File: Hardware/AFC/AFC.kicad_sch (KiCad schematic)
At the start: 5 parts, among them J1 Barrel_Jack_Switch, J2 Conn_Coaxial, J3 Conn_Coaxial, J4 Conn_Coaxial, J5 Conn_Coaxial

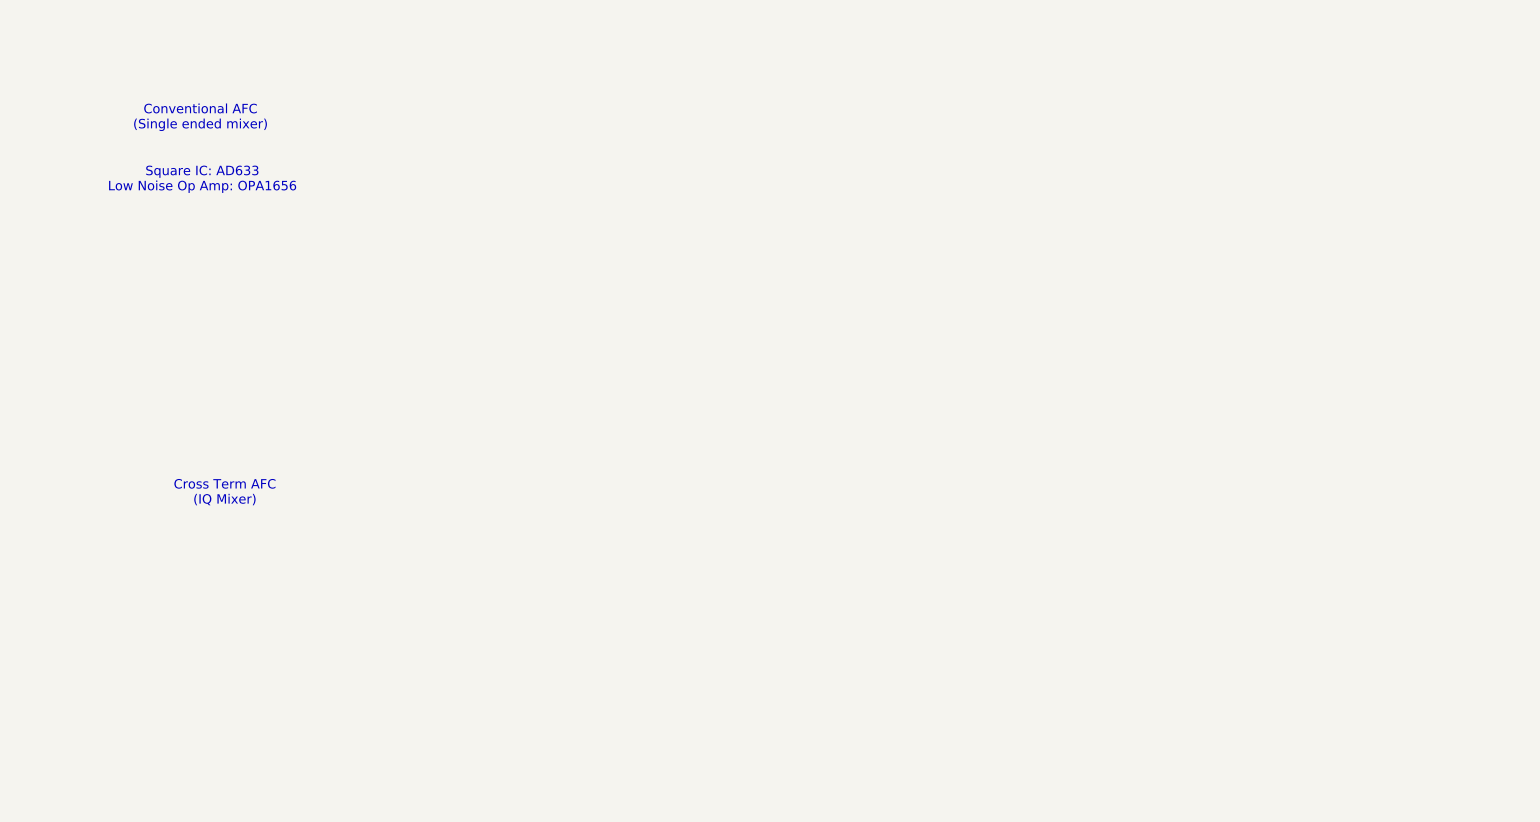
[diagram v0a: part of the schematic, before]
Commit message: Updating Schematic for AFC
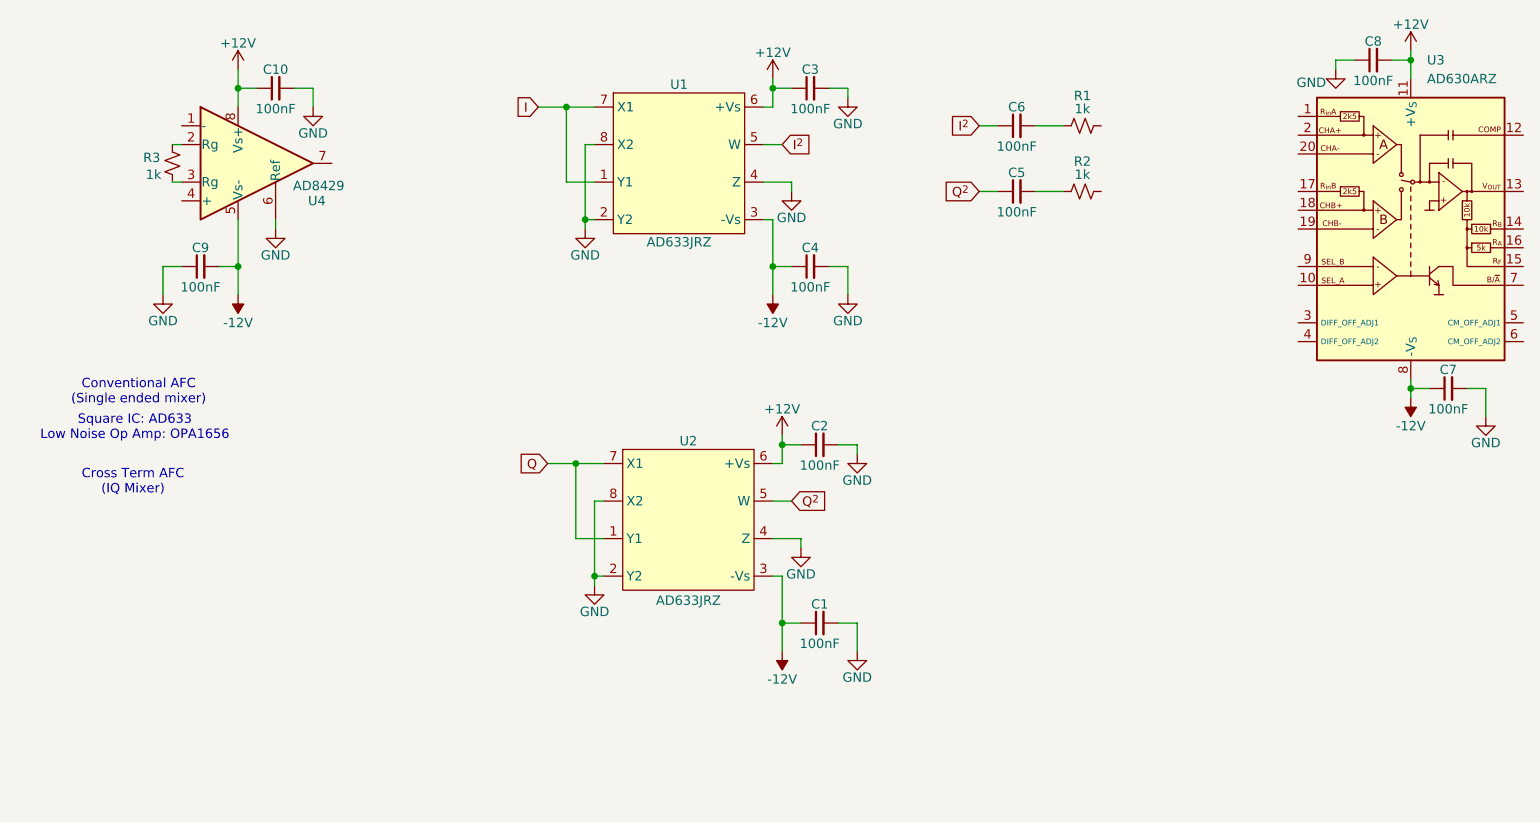
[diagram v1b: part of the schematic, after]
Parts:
- added C1, C10, C2, C3, C4, C5, C6, C7, C8, C9: 100nF, symbol Device:C_Small
- added R1, R2, R3: 1k, symbol Device:R_Small_US
- added U1, U2: AD633JRZ, Package_SO:SOIC-8_3.9x4.9mm_P1.27mm, symbol _tim-RF:AD633JRZ
- added U3: AD630ARZ, Package_SO:SOIC-20W_7.5x12.8mm_P1.27mm, symbol Analog:AD630ARZ
- added U4: AD8429, symbol Amplifier_Instrumentation:AD8429
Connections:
- net GND: now also C1.2, C10.2, C2.2, C3.2, C4.2, C7.2, C8.1, C9.1, U1.2 (Y2), U1.4 (Z), U1.8 (X2), U2.2 (Y2), U2.4 (Z), U2.8 (X2), U4.6 (Ref)
- net I: now also U1.1 (Y1), U1.7 (X1)
- net Q: now also U2.1 (Y1), U2.7 (X1)
- new net: C6.2, R1.1
- new net: C5.2, R2.1
- new net: R3.2, U4.2 (Rg)
- new net: R3.1, U4.3 (Rg)
- new net +12V: C10.1, C2.1, C3.1, C8.2, U1.6 (+Vs), U2.6 (+Vs), U3.11 (+V_{S}), U4.8 (Vs+)
- new net -12V: C1.1, C4.1, C7.1, C9.2, U1.3 (-Vs), U2.3 (-Vs), U3.8 (-V_{S}), U4.5 (Vs-)
- new net I^{2}: C6.1, U1.5 (W)
- new net Q^{2}: C5.1, U2.5 (W)

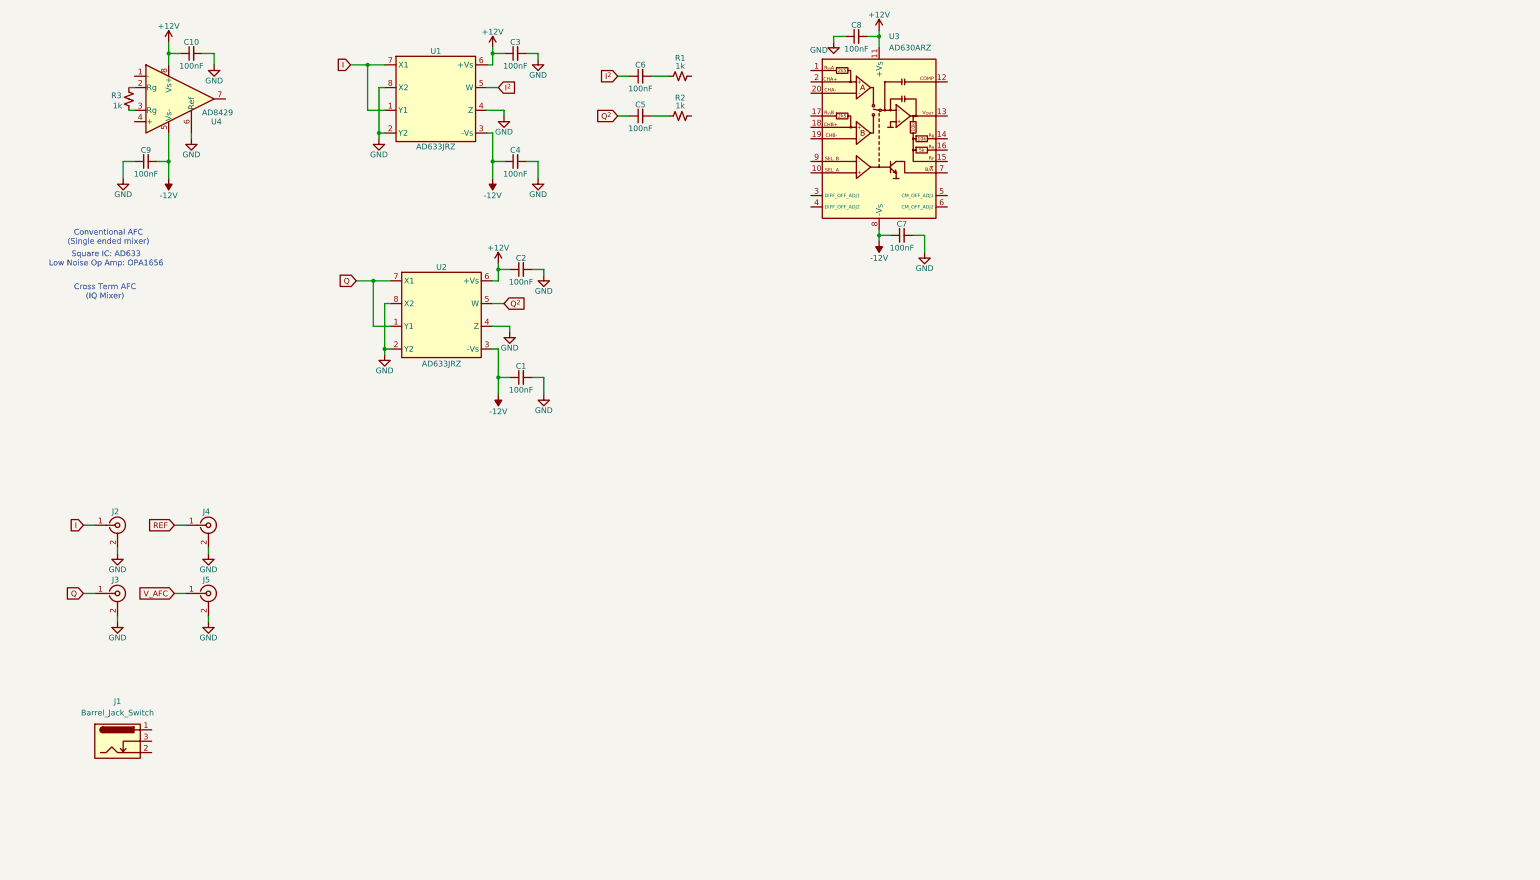
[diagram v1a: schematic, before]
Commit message: Updating Schematic for AFC Circuit
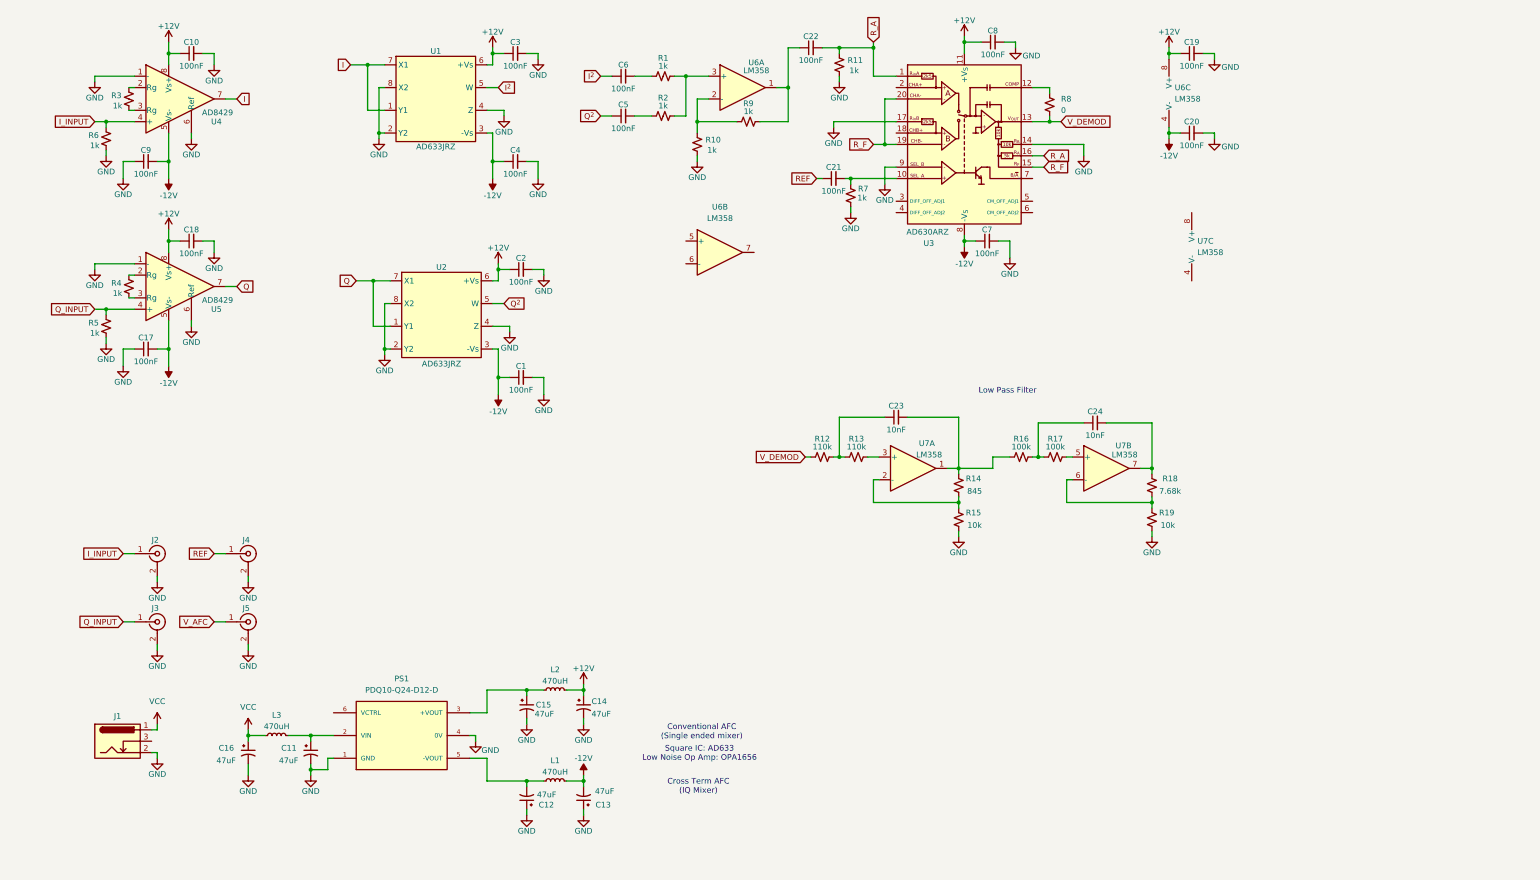
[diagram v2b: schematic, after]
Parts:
- added C11, C12, C13, C14, C15, C16: 47uF, symbol Device:C_Polarized_Small_US
- added C17, C18, C19, C20, C21, C22: 100nF, symbol Device:C_Small
- added C23, C24: 10nF, symbol Device:C_Small
- added L1, L2, L3: 470uH, symbol Device:L_Small
- added PS1: PDQ10-Q24-D12-D, symbol _tim-DC_DC:PDQE10-Q24-D5-D
- added R10, R11, R4, R5, R6, R7, R9: 1k, symbol Device:R_Small_US
- added R12, R13: 110k, symbol Device:R_Small_US
- added R14: 845, symbol Device:R_Small_US
- added R15, R19: 10k, symbol Device:R_Small_US
- added R16, R17: 100k, symbol Device:R_Small_US
- added R18: 7.68k, symbol Device:R_Small_US
- added R8: 0, symbol Device:R_Small_US
- added U5: AD8429, symbol Amplifier_Instrumentation:AD8429
- added U6, U7: LM358, Package_SO:SOIC-8_3.9x4.9mm_P1.27mm, symbol Amplifier_Operational:LM358
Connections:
- net +12V: now also C8.1, C14.1, C18.1, C19.1, L2.2, U5.8 (Vs+), U6.8 (V+); no longer C8.2
- net -12V: now also C13.2, C17.2, C20.1, L1.2, U5.5 (Vs-), U6.4 (V-)
- net GND: now also C8.2, J1.2, U3.14 (R_{B}), U3.17 (R_{in}B), U3.9 (SEL_B), U4.1 (-), C11.2, C12.1, C13.1, C14.2, C15.2, C16.2, C17.1, C18.2, C19.2, C20.2, PS1.1 (GND), PS1.4 (0V), R10.1, R11.1, R15.1, R19.1, R5.1, R6.1, R7.1, U5.1 (-), U5.6 (Ref); no longer C8.1
- net I: now also U4.7; no longer J2.1 (In)
- net Q: now also U5.7; no longer J3.1 (In)
- net REF: now also C21.1
- net at R1.2: now also R2.2, U6.3 (+)
- net R_A: now reaches U3.1 (R_{in}A)
- net R_A: now also U3.16 (R_{A}), C22.2, R11.2
- net at U3.10 (SEL_A): now also C21.2, R7.2
- net at U3.12 (COMP): now also R8.1
- net V_DEMOD: now reaches U3.13 (V_{OUT})
- net V_DEMOD: now also R12.1, R8.2
- net R_F: now reaches U3.15 (R_{F})
- net R_F: now also U3.19 (CHB-), U3.20 (CHA-)
- net I_INPUT: now reaches U4.4 (+)
- net I_INPUT: now also J2.1 (In), R6.2
- net VCC: now reaches J1.1
- net VCC: now also C16.1, L3.1
- new net: C23.1, R12.2, R13.1
- new net: R13.2, U7.3 (+)
- new net: R18.1, R19.2, U7.6 (-)
- new net: C24.2, R18.2, U7.7
- new net: C23.2, R14.2, R16.1, U7.1
- new net: R14.1, R15.2, U7.2 (-)
- new net: C11.1, L3.2, PS1.2 (VIN)
- new net: C22.1, R9.2, U6.1
- new net: R4.2, U5.2 (Rg)
- new net: R4.1, U5.3 (Rg)
- new net: C12.2, L1.1, PS1.5 (-VOUT)
- new net: R10.2, R9.1, U6.2 (-)
- new net: C24.1, R16.2, R17.1
- new net: R17.2, U7.5 (+)
- new net: C15.1, L2.1, PS1.3 (+VOUT)
- new net Q_INPUT: J3.1 (In), R5.2, U5.4 (+)
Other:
- note added: "Low Pass Filter"
- moved on the sheet: C5, C6, C7, C8, J2, J3, J4, J5, R1, R2, U3

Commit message: Updates to AFC schematic
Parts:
- removed C13, C14, C16: 47uF, symbol Device:C_Polarized_Small_US
- removed L1, L2, L3: 470uH, symbol Device:L_Small
- added C25, C26: 2.7nF, symbol Device:C_Small
- added C27, C28, C29: 100nF, symbol Device:C_Small
- added J6: Conn_Coaxial, symbol Connector:Conn_Coaxial
- added R20, R21, R22: 1k, symbol Device:R_Small_US
- added R23, R24, R25: 10k, symbol Device:R_Small_US
- R1, R10, R11, R2, R5, R6, R9: value 1k -> 10k
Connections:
- net +12V: now also C15.1, PS1.3 (+VOUT), U7.8 (V+), C28.1
- net -12V: now also C12.2, PS1.5 (-VOUT), U7.4 (V-), C27.1
- net GND: now also C25.1, C27.2, C28.2, J6.2 (Ext), R22.1, R24.1
- net VCC: now also C11.1, PS1.2 (VIN)
- net at R1.2, R2.2, U6.3 (+): now also R25.2
- net I^{2}+Q^{2}: now reaches R9.2, U6.1
- net I^{2}+Q^{2}: now also R20.1; no longer C22.1
- net at U6.5 (+): now also C25.2, C26.1, R22.2
- net at U6.6 (-): now also R23.1, R24.2
- net at U6.7: now also C22.1, R21.2, R23.2
- new net: C29.1, J6.1 (In)
- new net: C26.2, R20.2, R21.1
- new net Conventional: C29.2, R25.1
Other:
- note added: "70kHz Bandpass Filter"
- note added: "Adder"
- moved on the sheet: C1, C10, C17, C18, C19, C2, C20, C21, C22, C23, C24, C3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

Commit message: Adding filter to schematic
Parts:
- added C13, C14: 100pF, symbol Device:C_Small
- added R26, R27: 10k, symbol Device:R_Small_US
- added U8: LM358, Package_SO:SOIC-8_3.9x4.9mm_P1.27mm, symbol Amplifier_Operational:LM358
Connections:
- net GND: now also C13.1, C14.1
- net I: now also R27.2; no longer U1.1 (Y1), U1.7 (X1)
- net Q: now also R26.2; no longer U2.1 (Y1), U2.7 (X1)
- new net: C14.2, R27.1, U1.1 (Y1), U1.7 (X1)
- new net: C13.2, R26.1, U2.1 (Y1), U2.7 (X1)
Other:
- moved on the sheet: C1, C10, C17, C18, C2, C21, C22, C25, C26, C29, C3, C4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

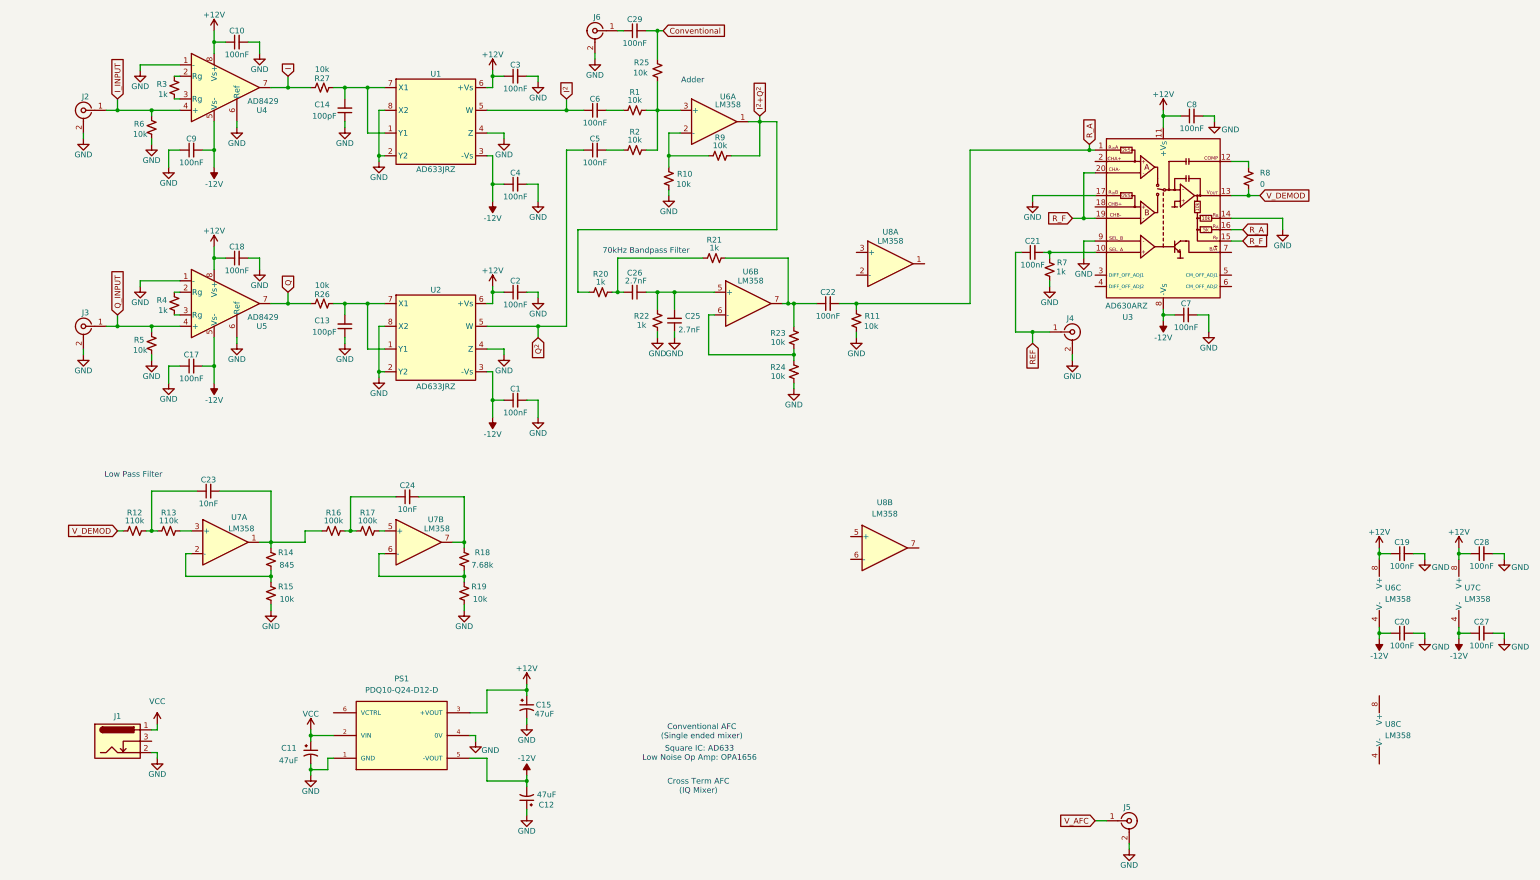
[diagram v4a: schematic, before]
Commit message: Adding amplifier
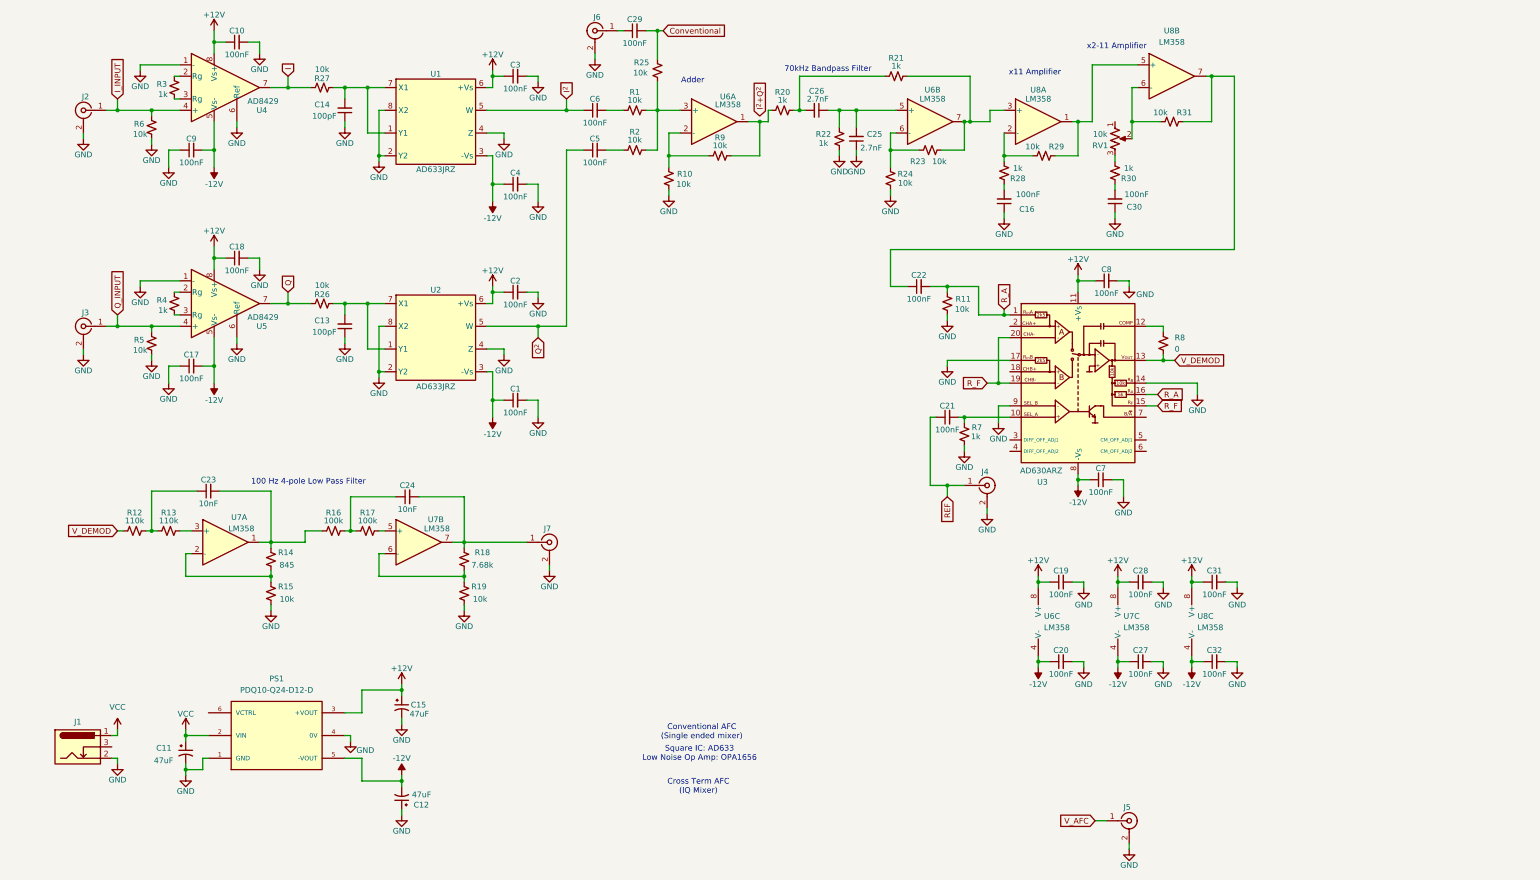
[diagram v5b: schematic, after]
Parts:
- added C16, C30, C31, C32: 100nF, symbol Device:C_Small
- added J7: Conn_Coaxial, symbol Connector:Conn_Coaxial
- added R28, R30: 1k, symbol Device:R_Small_US
- added R29, R31: 10k, symbol Device:R_Small_US
- added RV1: 10k, symbol Device:R_Potentiometer_US
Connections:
- net +12V: now also U8.8 (V+), C31.1
- net -12V: now also U8.4 (V-), C32.1
- net GND: now also C16.1, C30.1, C31.2, C32.2, J7.2 (Ext)
- net I^{2}+Q^{2}: no longer R20.1, R9.2, U6.1
- net at C24.2, R18.2, U7.7: now also J7.1 (In)
- net at U8.1: now also U8.5 (+), R29.2
- net at U8.2 (-): now also R28.1, R29.1
- net at U8.3 (+): now also R21.2, R23.1, U6.7
- net at U8.6 (-): now also R31.1, RV1.2
- net at U8.7: now also C22.1, R31.2
- net at R24.2, U6.6 (-): now also R23.2; no longer R23.1
- new net: R30.1, RV1.3
- new net: R20.1, R9.2, U6.1
- new net: C30.2, R30.2
- new net: C16.2, R28.2
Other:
- note added: "100 Hz 4-pole Low Pass Filter"
- note added: "x11 Amplifier"
- note added: "x2-11 Amplifier"
- note removed: "Low Pass Filter"
- moved on the sheet: C11, C12, C15, C19, C20, C21, C22, C25, C26, C27, C28, C7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
